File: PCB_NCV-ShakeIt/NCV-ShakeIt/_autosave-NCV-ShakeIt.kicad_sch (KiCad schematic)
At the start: 15 parts, among them U1 XIAO-SAMD21-DIP, U2 DFR0299

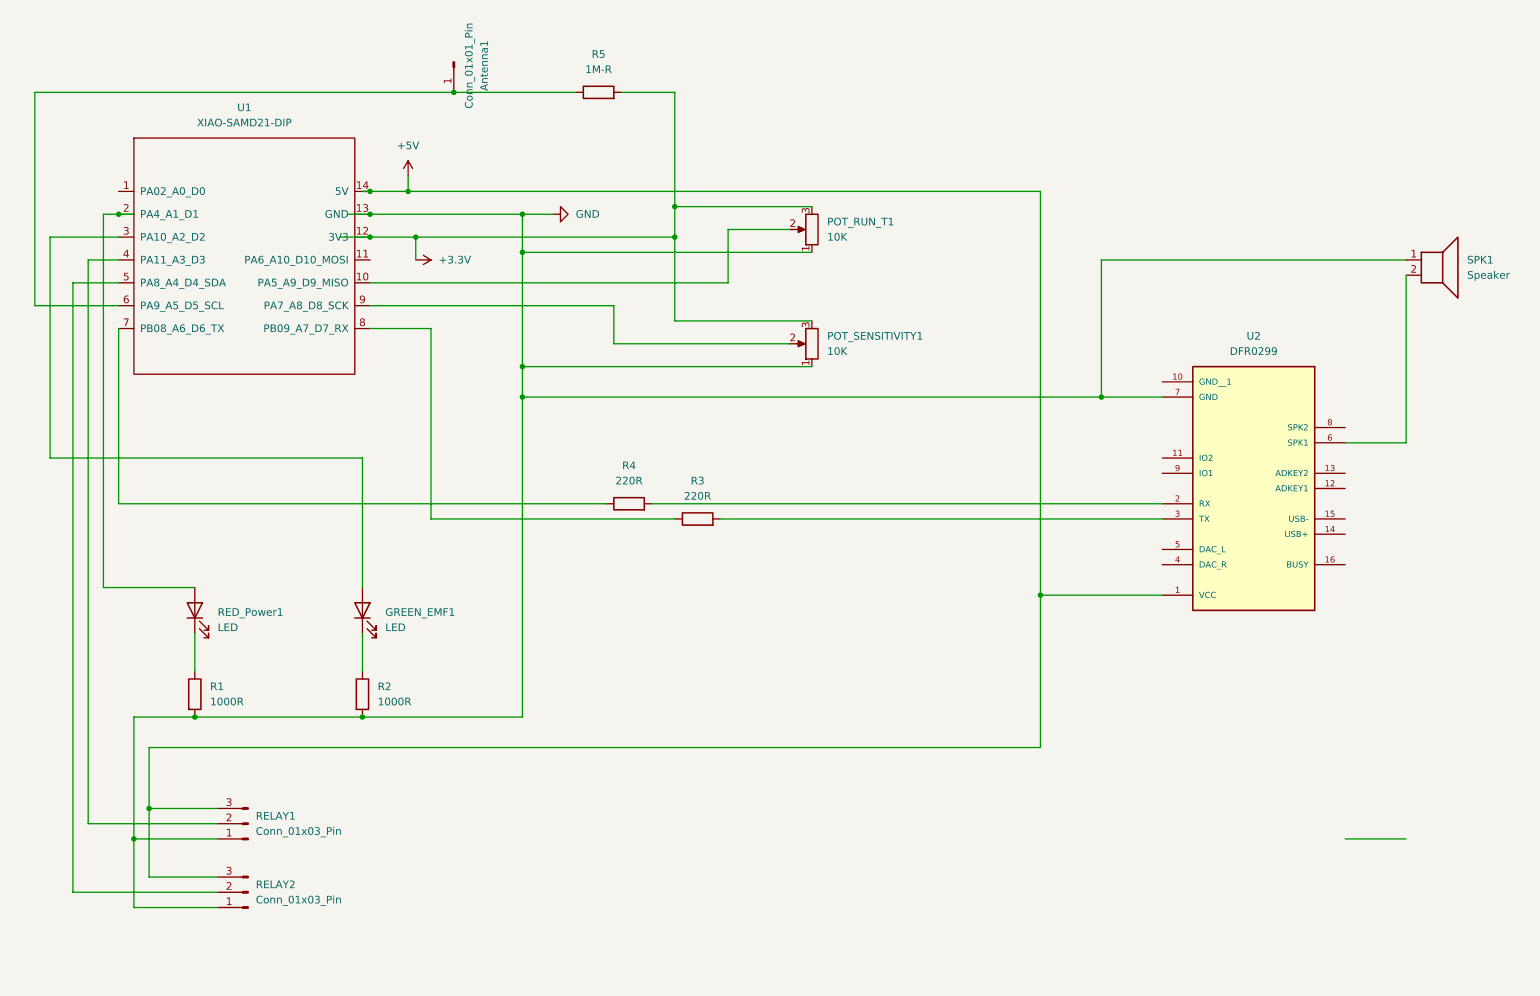
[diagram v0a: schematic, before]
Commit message: Adding to docs, fixing code, renaming things to be more clear
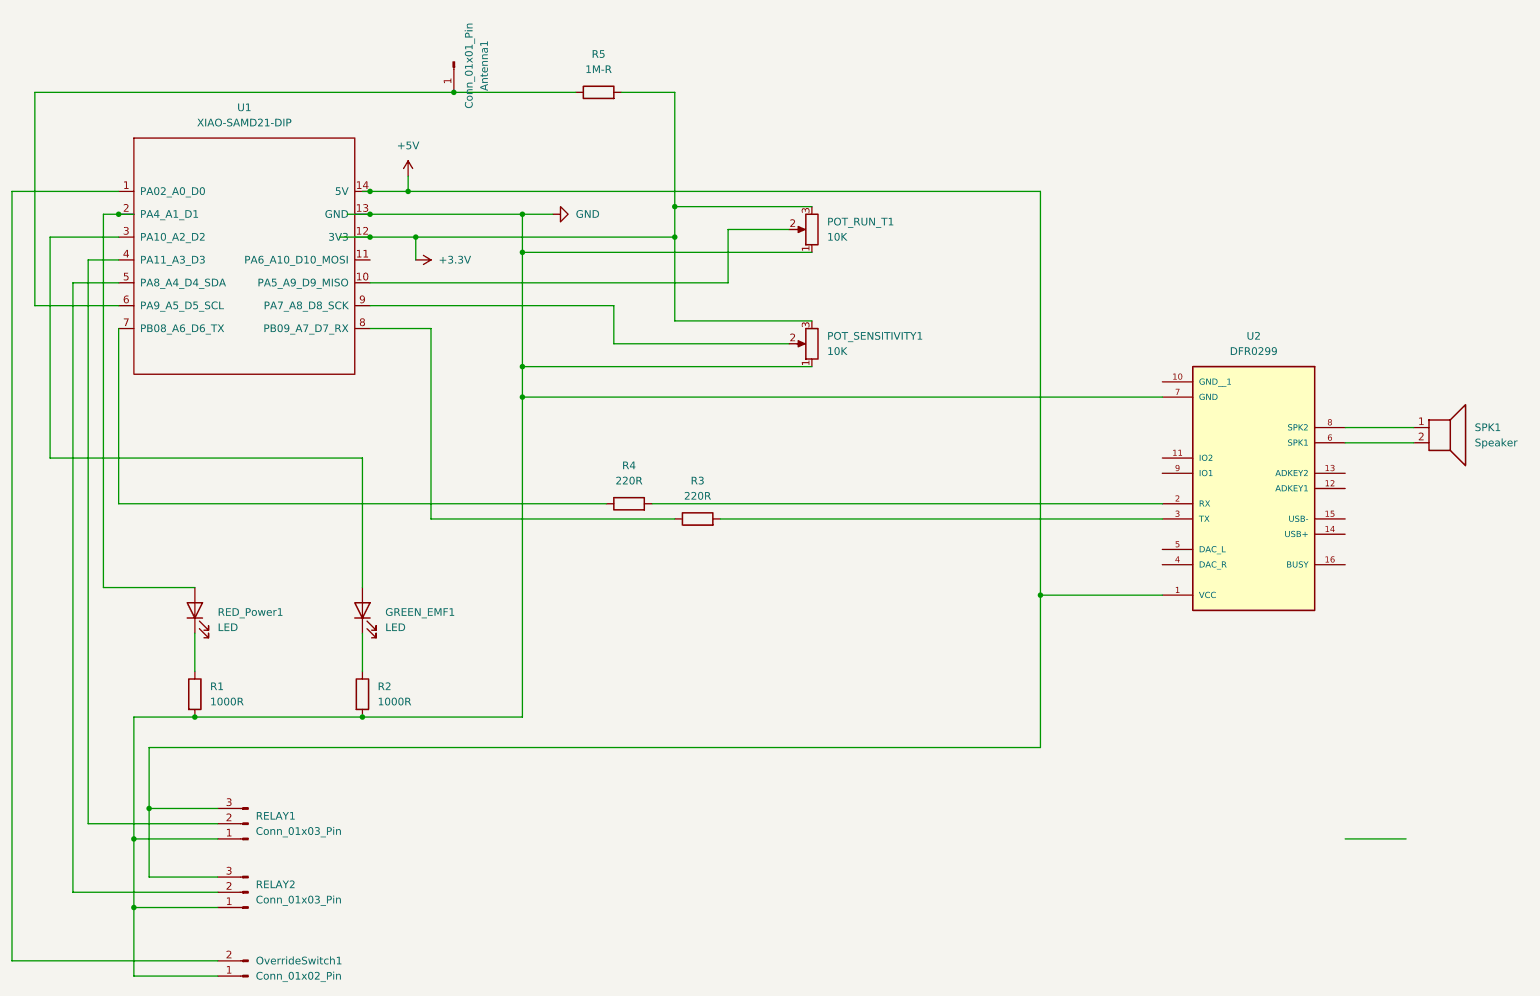
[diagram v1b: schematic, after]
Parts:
- added OverrideSwitch1: Conn_01x02_Pin, Connector_PinHeader_2.54mm:PinHeader_1x02_P2.54mm_Vertical, symbol Connector:Conn_01x02_Pin
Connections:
- net GND: now also OverrideSwitch1.1 (Pin_1); no longer SPK1.1
- net at U2.8 (SPK2): now also SPK1.1
- net at U1.1 (PA02_A0_D0): now also OverrideSwitch1.2 (Pin_2)
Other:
- moved on the sheet: SPK1
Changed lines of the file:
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@@
 	(generator_version "9.0")
 	(paper "A4")
+	(title_block
+		(rev "V2")
+	)
 	(junction
 		(at 36.83 149.86)
@@
 	)
 	(junction
-		(at 198.12 76.2)
+		(at 36.83 161.29)
 		(diameter 0)
 		(color 0 0 0 0)
@@
 	(wire
 		(pts
+			(xy 34.29 41.91) (xy 16.51 41.91)
+		)
+		(stroke
+			(width 0)
+			(type default)
+		)
+	)
+	(wire
+		(pts
 			(xy 86.36 64.77) (xy 86.36 96.52)
 		)
@@
 	(wire
 		(pts
+			(xy 238.76 81.28) (xy 250.19 81.28)
+		)
+		(stroke
+			(width 0)
+			(type default)
+		)
+	)
+	(wire
+		(pts
 			(xy 123.19 93.98) (xy 208.28 93.98)
 		)
@@
 	(wire
 		(pts
-			(xy 198.12 53.34) (xy 248.92 53.34)
-		)
-		(stroke
-			(width 0)
-			(type default)
-		)
-	)
-	(wire
-		(pts
-			(xy 101.6 76.2) (xy 198.12 76.2)
+			(xy 101.6 76.2) (xy 208.28 76.2)
 		)
 		(stroke
@@
 	(wire
 		(pts
+			(xy 16.51 41.91) (xy 16.51 170.18)
+		)
+		(stroke
+			(width 0)
+			(type default)
+		)
+	)
+	(wire
+		(pts
 			(xy 36.83 161.29) (xy 50.8 161.29)
 		)
@@
 	(wire
 		(pts
-			(xy 198.12 76.2) (xy 208.28 76.2)
-		)
-		(stroke
-			(width 0)
-			(type default)
-		)
-	)
-	(wire
-		(pts
 			(xy 82.55 41.91) (xy 187.96 41.91)
 		)
@@
 	(wire
 		(pts
-			(xy 248.92 83.82) (xy 248.92 55.88)
-		)
-		(stroke
-			(width 0)
-			(type default)
-		)
-	)
-	(wire
-		(pts
 			(xy 39.37 144.78) (xy 39.37 156.21)
 		)
@@
 	(wire
 		(pts
-			(xy 238.76 83.82) (xy 248.92 83.82)
+			(xy 238.76 83.82) (xy 250.19 83.82)
+		)
+		(stroke
+			(width 0)
+			(type default)
+		)
+	)
+	(wire
+		(pts
+			(xy 36.83 172.72) (xy 50.8 172.72)
+		)
+		(stroke
+			(width 0)
+			(type default)
+		)
+	)
+	(wire
+		(pts
+			(xy 36.83 161.29) (xy 36.83 172.72)
 		)
 		(stroke
@@
 	(wire
 		(pts
-			(xy 198.12 53.34) (xy 198.12 76.2)
-		)
-		(stroke
-			(width 0)
-			(type default)
-		)
-	)
-	(wire
-		(pts
 			(xy 101.6 45.72) (xy 106.68 45.72)
 		)
@@
 		(pts
 			(xy 82.55 39.37) (xy 82.55 41.91)
+		)
+		(stroke
+			(width 0)
+			(type default)
+		)
+	)
+	(wire
+		(pts
+			(xy 16.51 170.18) (xy 50.8 170.18)
 		)
 		(stroke
@@
 	)
 	(symbol
+		(lib_id "Connector:Conn_01x02_Pin")
+		(at 55.88 172.72 180)
+		(unit 1)
+		(exclude_from_sim no)
+		(in_bom yes)
+		(on_board yes)
+		(dnp no)
+		(fields_autoplaced yes)
+		(property "Reference" "OverrideSwitch1"
+			(at 57.15 170.1799 0)
+			(effects
+				(font
+					(size 1.27 1.27)
+				)
+				(justify right)
+			)
+		)
+		(property "Value" "Conn_01x02_Pin"
+			(at 57.15 172.7199 0)
+			(effects
+				(font
+					(size 1.27 1.27)
+				)
+				(justify right)
+			)
+		)
+		(property "Footprint" "Connector_PinHeader_2.54mm:PinHeader_1x02_P2.54mm_Vertical"
+			(at 55.88 172.72 0)
+			(effects
+				(font
+					(size 1.27 1.27)
+				)
+				(hide yes)
+			)
+		)
+		(property "Datasheet" "~"
+			(at 55.88 172.72 0)
+			(effects
+				(font
+					(size 1.27 1.27)
+				)
+				(hide yes)
+			)
+		)
+		(property "Description" "Generic connector, single row, 01x02, script generated"
+			(at 55.88 172.72 0)
+			(effects
+				(font
+					(size 1.27 1.27)
+				)
+				(hide yes)
+			)
+		)
+		(pin "1"
+		)
+		(pin "2"
+		)
+		(instances
+			(project ""
+				(path "/7725b597-6567-4f6d-8f5d-b74a617fc15f"
+					(reference "OverrideSwitch1")
+					(unit 1)
+				)
+			)
+		)
+	)
+	(symbol
 		(lib_id "Device:Speaker")
-		(at 254 53.34 0)
+		(at 255.27 81.28 0)
 		(unit 1)
 		(exclude_from_sim no)
@@
 		(fields_autoplaced yes)
 		(property "Reference" "SPK1"
-			(at 259.08 53.3399 0)
+			(at 260.35 81.2799 0)
 			(effects
 				(font
@@
 		)
 		(property "Value" "Speaker"
-			(at 259.08 55.8799 0)
+			(at 260.35 83.8199 0)
 			(effects
 				(font
@@
 		)
 		(property "Footprint" "Connector_PinHeader_2.54mm:PinHeader_1x02_P2.54mm_Vertical"
-			(at 254 58.42 0)
+			(at 255.27 86.36 0)
 			(effects
 				(font
@@
 		)
 		(property "Datasheet" "~"
-			(at 253.746 54.61 0)
+			(at 255.016 82.55 0)
 			(effects
 				(font
@@
 		)
 		(property "Description" "Speaker"
-			(at 254 53.34 0)
-			(effects
-				(font
+			(at 255.27 81.28 0)
+			(effects
+				(font
